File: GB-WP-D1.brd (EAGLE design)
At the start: 25.5 x 36.5 mm, 10 parts

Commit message: Add files via upload
GND layers
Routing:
- net D6: track 27.5 -> 26.7 mm
- added copper zone on layer 1, net GND
- added copper zone on layer 16, net GND
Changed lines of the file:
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@@
 <setting verticaltext="up"/>
 </settings>
-<grid distance="0.000417" unitdist="inch" unit="inch" style="lines" multiple="1" display="yes" altdistance="5" altunitdist="mil" altunit="mil"/>
+<grid distance="5" unitdist="mil" unit="mil" style="lines" multiple="1" display="yes" altdistance="5" altunitdist="mil" altunit="mil"/>
 <layers>
 <layer number="1" name="Top" color="4" fill="1" visible="yes" active="yes"/>
@@
 <wire x1="19.939" y1="8.2042" x2="21.59" y2="9.8552" width="0.2032" layer="16"/>
 <wire x1="15.24" y1="4.9791875" x2="18.3888125" y2="8.128" width="0.2032" layer="1"/>
+<polygon width="0.1524" layer="16">
+<vertex x="-0.635" y="-1.143"/>
+<vertex x="-0.635" y="37.084"/>
+<vertex x="9.271" y="37.084"/>
+<vertex x="9.271" y="30.988"/>
+<vertex x="16.51" y="30.988"/>
+<vertex x="16.51" y="37.338"/>
+<vertex x="26.924" y="37.084"/>
+<vertex x="26.924" y="-1.143"/>
+</polygon>
+<polygon width="0.1524" layer="1">
+<vertex x="9.271" y="30.988"/>
+<vertex x="16.383" y="30.988"/>
+<vertex x="16.383" y="37.338"/>
+<vertex x="27.051" y="37.338"/>
+<vertex x="27.051" y="-1.016"/>
+<vertex x="-0.635" y="-1.016"/>
+<vertex x="-0.635" y="36.957"/>
+<vertex x="9.271" y="36.957"/>
+</polygon>
 </signal>
 <signal name="D2">
@@
 <contactref element="JP4" pad="3"/>
 <wire x1="14.594084375" y1="33.7970875" x2="14.594084375" y2="31.0980875" width="0.2032" layer="1"/>
-<wire x1="13.229084375" y1="29.7330875" x2="12.086084375" y2="29.7330875" width="0.2032" layer="1"/>
-<wire x1="12.086084375" y1="29.7330875" x2="11.324084375" y2="28.9710875" width="0.2032" layer="1"/>
+<wire x1="12.594084375" y1="29.0980875" x2="11.451084375" y2="29.0980875" width="0.2032" layer="1"/>
+<wire x1="11.451084375" y1="29.0980875" x2="11.324084375" y2="28.9710875" width="0.2032" layer="1"/>
 <wire x1="11.324084375" y1="28.9710875" x2="11.324084375" y2="27.7010875" width="0.2032" layer="1"/>
-<wire x1="14.594084375" y1="31.0980875" x2="13.229084375" y2="29.7330875" width="0.2032" layer="1"/>
+<wire x1="14.594084375" y1="31.0980875" x2="12.594084375" y2="29.0980875" width="0.2032" layer="1"/>
 <wire x1="11.324084375" y1="27.7010875" x2="11.324084375" y2="24.024084375" width="0.2032" layer="1"/>
 <wire x1="4.7752" y1="17.4752" x2="11.324084375" y2="24.024084375" width="0.2032" layer="1"/>
@@
 <contactref element="JP4" pad="4"/>
 <wire x1="10.594084375" y1="33.7970875" x2="10.594084375" y2="31.0980875" width="0.2032" layer="16"/>
-<wire x1="10.594084375" y1="31.0980875" x2="11.959084375" y2="29.7330875" width="0.2032" layer="16"/>
-<wire x1="11.959084375" y1="29.7330875" x2="13.229084375" y2="29.7330875" width="0.2032" layer="16"/>
-<wire x1="13.229084375" y1="29.7330875" x2="13.864084375" y2="29.0980875" width="0.2032" layer="16"/>
-<wire x1="13.864084375" y1="29.0980875" x2="13.864084375" y2="27.7010875" width="0.2032" layer="16"/>
+<wire x1="10.594084375" y1="31.0980875" x2="13.864084375" y2="27.8280875" width="0.2032" layer="16"/>
+<wire x1="13.864084375" y1="27.8280875" x2="13.864084375" y2="27.7010875" width="0.2032" layer="16"/>
 <wire x1="13.864084375" y1="27.7010875" x2="13.864084375" y2="25.294084375" width="0.2032" layer="1"/>
 <wire x1="3.5052" y1="14.9352" x2="13.864084375" y2="25.294084375" width="0.2032" layer="1"/>
@@
 <contactref element="U$2" pad="3"/>
 <contactref element="JP4" pad="2"/>
-<wire x1="12.594084375" y1="33.7970875" x2="12.594084375" y2="31.1300875" width="0.2032" layer="1"/>
-<wire x1="12.594084375" y1="31.1300875" x2="11.197084375" y2="29.7330875" width="0.2032" layer="1"/>
-<wire x1="11.197084375" y1="29.7330875" x2="9.800084375" y2="29.7330875" width="0.2032" layer="1"/>
-<wire x1="9.800084375" y1="29.7330875" x2="8.784084375" y2="28.7170875" width="0.2032" layer="1"/>
+<wire x1="12.594084375" y1="33.7970875" x2="12.594084375" y2="31.6380875" width="0.2032" layer="1"/>
+<wire x1="12.594084375" y1="31.6380875" x2="10.181084375" y2="29.2250875" width="0.2032" layer="1"/>
+<wire x1="10.181084375" y1="29.2250875" x2="9.292084375" y2="29.2250875" width="0.2032" layer="1"/>
+<wire x1="9.292084375" y1="29.2250875" x2="8.784084375" y2="28.7170875" width="0.2032" layer="1"/>
 <wire x1="8.784084375" y1="27.7010875" x2="8.784084375" y2="22.881084375" width="0.2032" layer="1"/>
 <wire x1="8.784084375" y1="22.881084375" x2="4.318" y2="18.415" width="0.2032" layer="1"/>
@@
 <contactref element="U$2" pad="4"/>
 <contactref element="JP4" pad="5"/>
-<wire x1="12.594084375" y1="33.7970875" x2="12.594084375" y2="31.1300875" width="0.2032" layer="16"/>
-<wire x1="13.991084375" y1="29.7330875" x2="15.388084375" y2="29.7330875" width="0.2032" layer="16"/>
+<wire x1="12.594084375" y1="33.7970875" x2="12.594084375" y2="31.2570875" width="0.2032" layer="16"/>
+<wire x1="14.118084375" y1="29.7330875" x2="12.594084375" y2="31.2570875" width="0.2032" layer="16"/>
+<wire x1="14.118084375" y1="29.7330875" x2="15.388084375" y2="29.7330875" width="0.2032" layer="16"/>
 <wire x1="15.388084375" y1="29.7330875" x2="16.404084375" y2="28.7170875" width="0.2032" layer="16"/>
 <wire x1="16.404084375" y1="28.7170875" x2="16.404084375" y2="27.7010875" width="0.2032" layer="16"/>
-<wire x1="12.594084375" y1="31.1300875" x2="13.991084375" y2="29.7330875" width="0.2032" layer="16"/>
 <contactref element="4.7K" pad="1"/>
 <wire x1="16.404084375" y1="27.7010875" x2="18.152878125" y2="25.95229375" width="0.2032" layer="16"/>

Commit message: Add files via upload
SMT Jumpers for the OLED's GND and VCC
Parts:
- added JP2, JP5: JUMPER-SMT_3_NO_NO-SILK, SparkFun-Jumpers:SMT-JUMPER_3_NO_NO-SILK
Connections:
- new net N$2: JP1.3, JP5.2
- new net N$3: JP1.4, JP2.2
- net 3.3V: now also JP2.1, JP5.1; no longer JP1.3
- net GND: now also JP2.3, JP5.3; no longer JP1.4
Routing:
- net N$2: track 0.00 -> 6.26 mm
- net N$3: track 0.00 -> 5.84 mm
- net 3.3V: track 55.6 -> 54.5 mm, vias 0 -> 2
- net GND: track 44.6 -> 44.3 mm, vias 1 -> 0
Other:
- board text added: "J1"
- board text added: "J2"
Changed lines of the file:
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@@
 <text x="8.001" y="2.413" size="0.8128" layer="21" font="vector" ratio="15" rot="R90">SDA</text>
 <text x="10.541" y="2.413" size="0.8128" layer="21" font="vector" ratio="15" rot="R90">SCL</text>
-<text x="13.081" y="2.413" size="0.8128" layer="21" font="vector" ratio="15" rot="R90">VCC</text>
-<text x="15.621" y="2.413" size="0.8128" layer="21" font="vector" ratio="15" rot="R90">GND</text>
+<text x="13.081" y="2.413" size="0.8128" layer="21" font="vector" ratio="15" rot="R90">J2</text>
+<text x="15.621" y="2.413" size="0.8128" layer="21" font="vector" ratio="15" rot="R90">J1</text>
 <text x="7.192728125" y="17.109596875" size="0.762" layer="22" font="vector" ratio="12" distance="25" rot="SMR270" align="center">https://git.io/JJk92
 https://bit.ly/gbccd
@@
 <text x="18.563084375" y="26.6850875" size="0.889" layer="22" font="vector" ratio="15" rot="MR90" align="bottom-right">GND</text>
 <text x="5.736084375" y="28.7170875" size="1.016" layer="21" font="vector" ratio="20">GB</text>
-<wire x1="21.992084375" y1="34.1780875" x2="21.992084375" y2="33.4160875" width="0.1524" layer="21"/>
-<wire x1="21.611084375" y1="33.7970875" x2="22.373084375" y2="33.7970875" width="0.1524" layer="21"/>
+<wire x1="19.452084375" y1="35.1940875" x2="19.452084375" y2="34.4320875" width="0.1524" layer="21"/>
+<wire x1="19.071084375" y1="34.8130875" x2="19.833084375" y2="34.8130875" width="0.1524" layer="21"/>
 <rectangle x1="9.396446875" y1="8.490865625" x2="9.480265625" y2="8.501534375" layer="25" rot="R90" grouprefs="GBPRINTER_2"/>
 <rectangle x1="9.3274875" y1="8.496071875" x2="9.52814375" y2="8.506484375" layer="25" rot="R90" grouprefs="GBPRINTER_2"/>
@@
 <text x="10.40114375" y="11.61920625" size="1.016" layer="25" rot="R90">4 WEMOS D1 mini</text>
 <hole x="3.67535625" y="32.463865625" drill="3.81"/>
+<wire x1="19.071084375" y1="30.2410875" x2="19.833084375" y2="30.2410875" width="0.1524" layer="21"/>
+<text x="10.922" y="6.096" size="0.8128" layer="22" font="vector" ratio="15" rot="MR180">J2</text>
+<text x="14.478" y="6.096" size="0.8128" layer="22" font="vector" ratio="15" rot="MR180">J1</text>
 </plain>
 <attributes>
@@
 </element>
 <element name="R1" library="SparkFun-Resistors" package="1206" value="4.7KOHM" x="10.26345625" y="9.62794375" smashed="yes" rot="MR0"/>
+<element name="JP2" library="SparkFun-Jumpers" package="SMT-JUMPER_3_NO_NO-SILK" value="JUMPER-SMT_3_NO_NO-SILK" x="15.24" y="7.112" smashed="yes" rot="MR180"/>
+<element name="JP5" library="SparkFun-Jumpers" package="SMT-JUMPER_3_NO_NO-SILK" value="JUMPER-SMT_3_NO_NO-SILK" x="11.684" y="7.112" smashed="yes" rot="MR180"/>
 </elements>
 <signals>
@@
 </signal>
 <signal name="GND">
-<contactref element="JP1" pad="4"/>
 <contactref element="U$2" pad="6"/>
 <contactref element="JP4" pad="6"/>
@@
 <wire x1="18.944084375" y1="27.7010875" x2="18.944084375" y2="14.075915625" width="0.2032" layer="16"/>
 <wire x1="18.944084375" y1="14.075915625" x2="23.1648" y2="9.8552" width="0.2032" layer="16"/>
-<wire x1="15.24" y1="1.27" x2="15.24" y2="4.9791875" width="0.2032" layer="1"/>
-<wire x1="21.59" y1="9.8552" x2="24.13" y2="9.8552" width="0.2032" layer="16"/>
-<wire x1="18.3888125" y1="8.128" x2="19.939" y2="8.128" width="0.2032" layer="1"/>
-<via x="19.939" y="8.128" extent="1-16" drill="0.3556"/>
-<wire x1="19.939" y1="8.128" x2="19.939" y2="8.2042" width="0.2032" layer="16"/>
-<wire x1="19.939" y1="8.2042" x2="21.59" y2="9.8552" width="0.2032" layer="16"/>
-<wire x1="15.24" y1="4.9791875" x2="18.3888125" y2="8.128" width="0.2032" layer="1"/>
 <polygon width="0.1524" layer="16">
 <vertex x="-0.635" y="-1.143"/>
-<vertex x="-0.635" y="37.084"/>
-<vertex x="9.271" y="37.084"/>
+<vertex x="-0.635" y="37.465"/>
+<vertex x="9.271" y="37.465"/>
 <vertex x="9.271" y="30.988"/>
 <vertex x="16.51" y="30.988"/>
@@
 <vertex x="9.271" y="36.957"/>
 </polygon>
+<contactref element="JP5" pad="3"/>
+<contactref element="JP2" pad="3"/>
+<wire x1="24.13" y1="9.8552" x2="18.9992" y2="9.8552" width="0.2032" layer="16"/>
+<wire x1="17.399" y1="8.255" x2="16.256" y2="8.255" width="0.2032" layer="16"/>
+<wire x1="16.256" y1="8.255" x2="12.954" y2="8.255" width="0.2032" layer="16"/>
+<wire x1="16.0528" y1="7.112" x2="16.0528" y2="8.0518" width="0.2032" layer="16"/>
+<wire x1="18.9992" y1="9.8552" x2="17.399" y2="8.255" width="0.2032" layer="16"/>
+<wire x1="12.954" y1="8.255" x2="12.4968" y2="7.7978" width="0.2032" layer="16"/>
+<wire x1="12.4968" y1="7.7978" x2="12.4968" y2="7.112" width="0.2032" layer="16"/>
+<wire x1="16.0528" y1="8.0518" x2="16.256" y2="8.255" width="0.2032" layer="16"/>
 </signal>
 <signal name="D2">
@@
 <contactref element="JP3" pad="8"/>
 <wire x1="1.27" y1="7.3152" x2="2.2352" y2="7.3152" width="0.2032" layer="1"/>
-<contactref element="JP1" pad="3"/>
-<wire x1="1.27" y1="7.3152" x2="9.1035625" y2="7.3152" width="0.2032" layer="16"/>
-<wire x1="12.7" y1="3.7187625" x2="9.1035625" y2="7.3152" width="0.2032" layer="16"/>
-<wire x1="12.7" y1="1.27" x2="12.7" y2="3.7187625" width="0.2032" layer="16"/>
 <wire x1="21.123559375" y1="33.745040625" x2="20.16351875" y2="32.785" width="0.2032" layer="1"/>
 <wire x1="20.16351875" y1="32.785" x2="20.16351875" y2="26.7242375" width="0.2032" layer="1"/>
@@
 <wire x1="23.895103125" y1="34.006234375" x2="23.8881125" y2="33.99924375" width="0.2032" layer="1"/>
 <wire x1="23.8881125" y1="33.99924375" x2="21.3777625" y2="33.99924375" width="0.2032" layer="1"/>
+<contactref element="JP5" pad="1"/>
+<contactref element="JP2" pad="1"/>
+<wire x1="1.27" y1="7.3152" x2="9.7028" y2="7.3152" width="0.2032" layer="1"/>
+<wire x1="9.7028" y1="7.3152" x2="9.906" y2="7.112" width="0.2032" layer="1"/>
+<via x="9.906" y="7.112" extent="1-16" drill="0.3556"/>
+<wire x1="9.906" y1="7.112" x2="10.8712" y2="7.112" width="0.2032" layer="16"/>
+<wire x1="9.906" y1="7.112" x2="13.335" y2="7.112" width="0.2032" layer="1"/>
+<wire x1="13.335" y1="7.112" x2="13.462" y2="6.985" width="0.2032" layer="1"/>
+<via x="13.462" y="6.985" extent="1-16" drill="0.3556"/>
+<wire x1="13.462" y1="6.985" x2="13.589" y2="7.112" width="0.2032" layer="16"/>
+<wire x1="13.589" y1="7.112" x2="14.4272" y2="7.112" width="0.2032" layer="16"/>
 </signal>
 <signal name="N$1">
@@
 <contactref element="JP6" pad="2"/>
 </signal>
+<signal name="N$2">
+<contactref element="JP1" pad="3"/>
+<contactref element="JP5" pad="2"/>
+<wire x1="11.684" y1="7.112" x2="11.9253" y2="6.8707" width="0.2032" layer="16"/>
+<wire x1="11.9253" y1="6.8707" x2="11.9253" y2="6.3717875" width="0.2032" layer="16"/>
+<wire x1="12.7" y1="5.5970875" x2="12.7" y2="1.27" width="0.2032" layer="16"/>
+<wire x1="11.9253" y1="6.3717875" x2="12.7" y2="5.5970875" width="0.2032" layer="16"/>
+</signal>
+<signal name="N$3">
+<contactref element="JP2" pad="2"/>
+<contactref element="JP1" pad="4"/>
+<wire x1="15.24" y1="7.112" x2="15.24" y2="1.27" width="0.2032" layer="16"/>
+</signal>
 </signals>

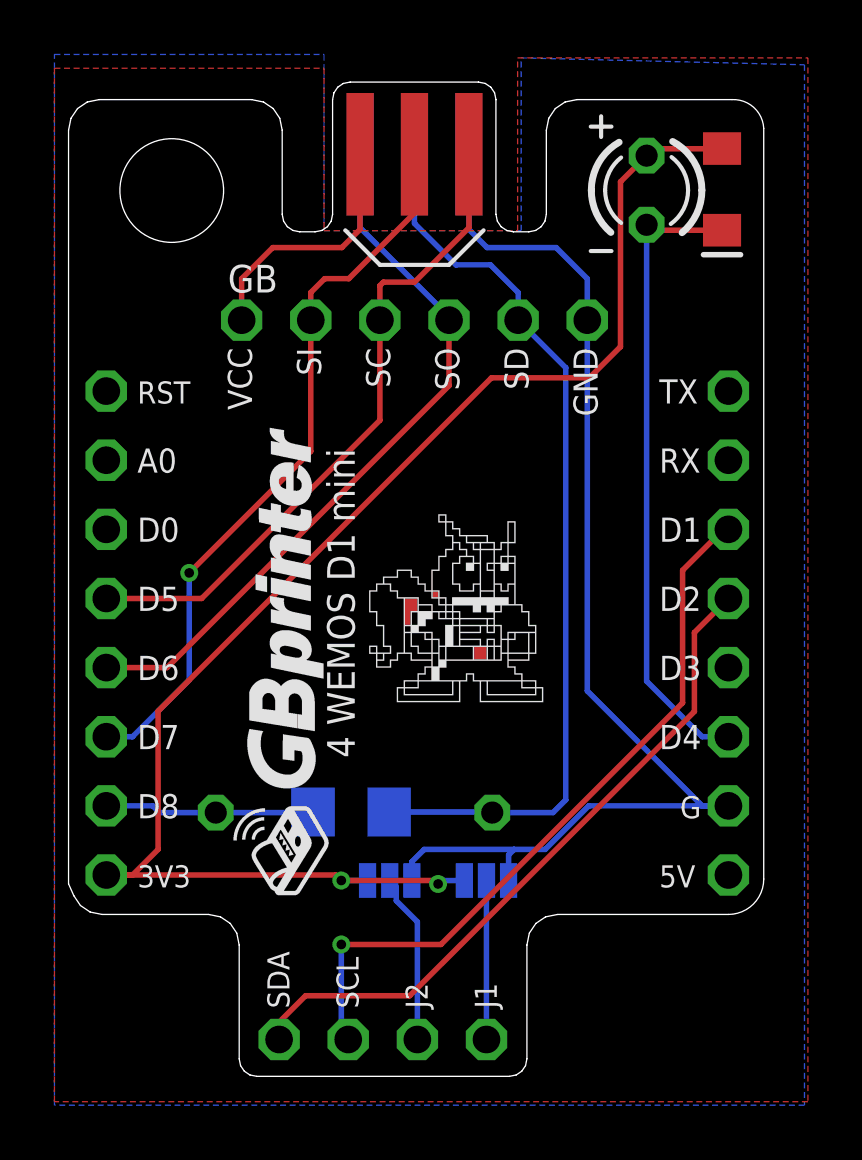
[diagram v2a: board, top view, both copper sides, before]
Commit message: Add files via upload
Unnecesari SMT Jumper config for OLED 128x32
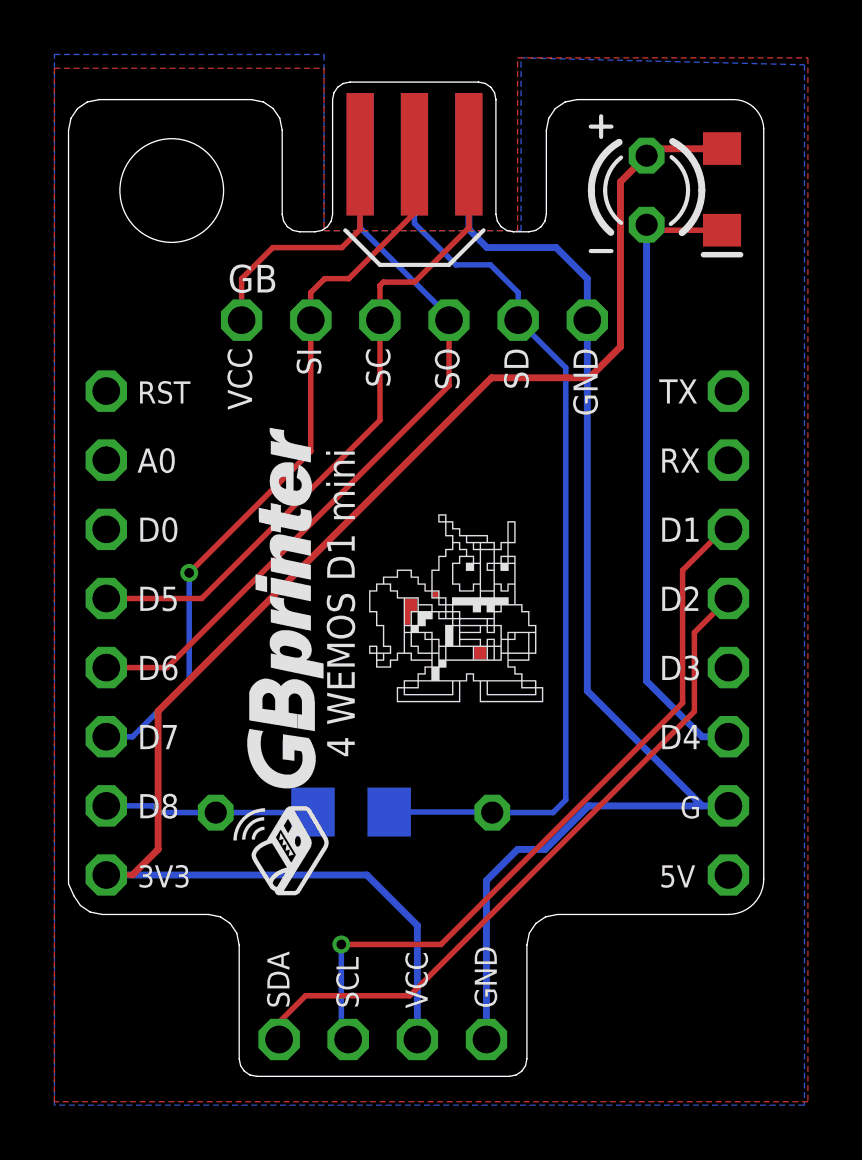
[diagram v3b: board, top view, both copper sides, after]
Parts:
- removed JP2, JP5: JUMPER-SMT_3_NO_NO-SILK, SparkFun-Jumpers:SMT-JUMPER_3_NO_NO-SILK
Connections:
- removed net N$2: JP1.3, JP5.2
- removed net N$3: JP1.4, JP2.2
- net 3.3V: now also JP1.3; no longer JP2.1, JP5.1
- net GND: now also JP1.4; no longer JP2.3, JP5.3
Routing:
- net N$2: track 6.26 -> 0.00 mm
- net N$3: track 5.84 -> 0.00 mm
- net 3.3V: track 54.5 -> 56.6 mm, vias 2 -> 0
- net GND: track 44.3 -> 45.8 mm
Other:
- board text removed: "J1"
- board text removed: "J2"
